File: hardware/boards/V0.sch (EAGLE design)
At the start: 100 parts, among them IC2 TPS6300, J1 SJ-43515TS-SMT, J2 HIROSE_DM3BT-DSF-PEJSHIROSE_D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, J3 MOLEX_105450-0101MOLEX_105450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, Q1 MC-306, Q2 ON_SEMI_MMBT5551LT1GON_SEMI_M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, U1 VS1053-L, U2 MICROCHIP_MCP73831T-2ATI-OTMI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, X1 PG203J, X3 FH12-45S-0.5SH

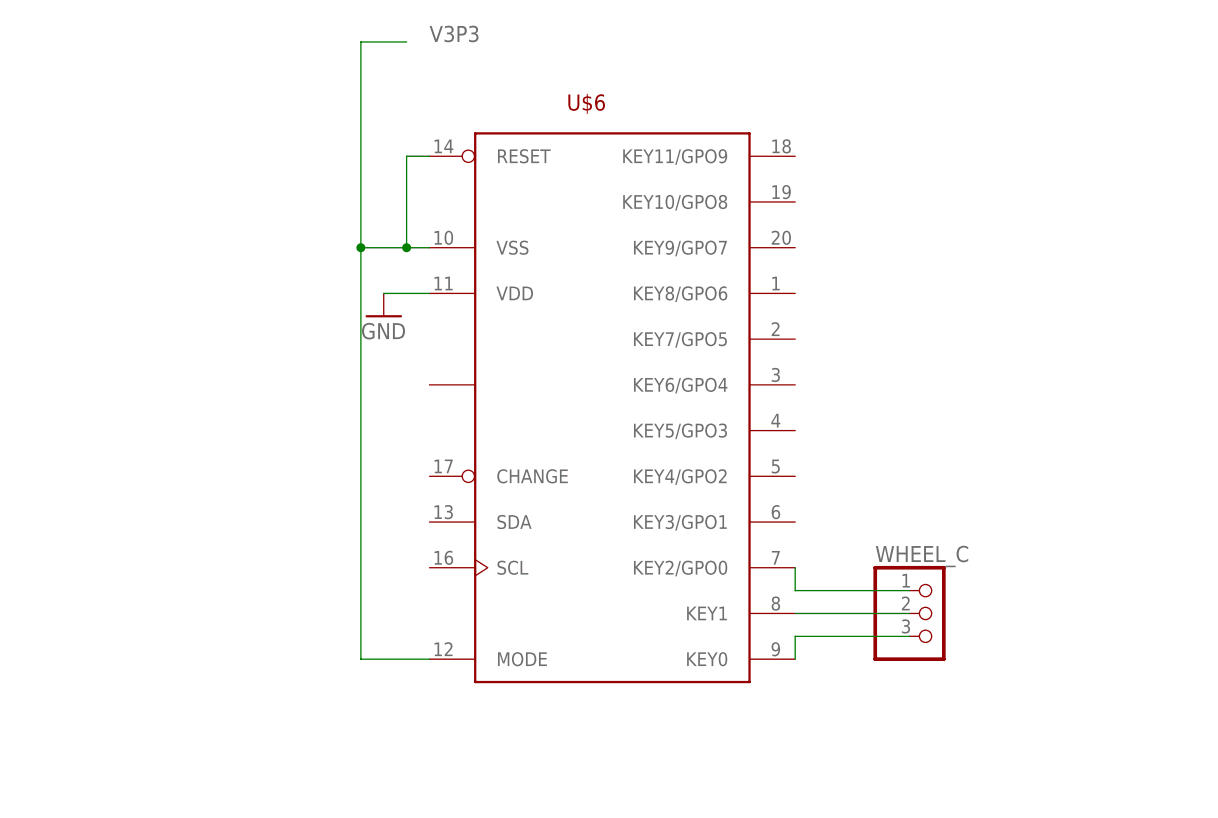
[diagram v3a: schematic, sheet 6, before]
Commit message: misc VS1053 fixes + fix/wire ATQ
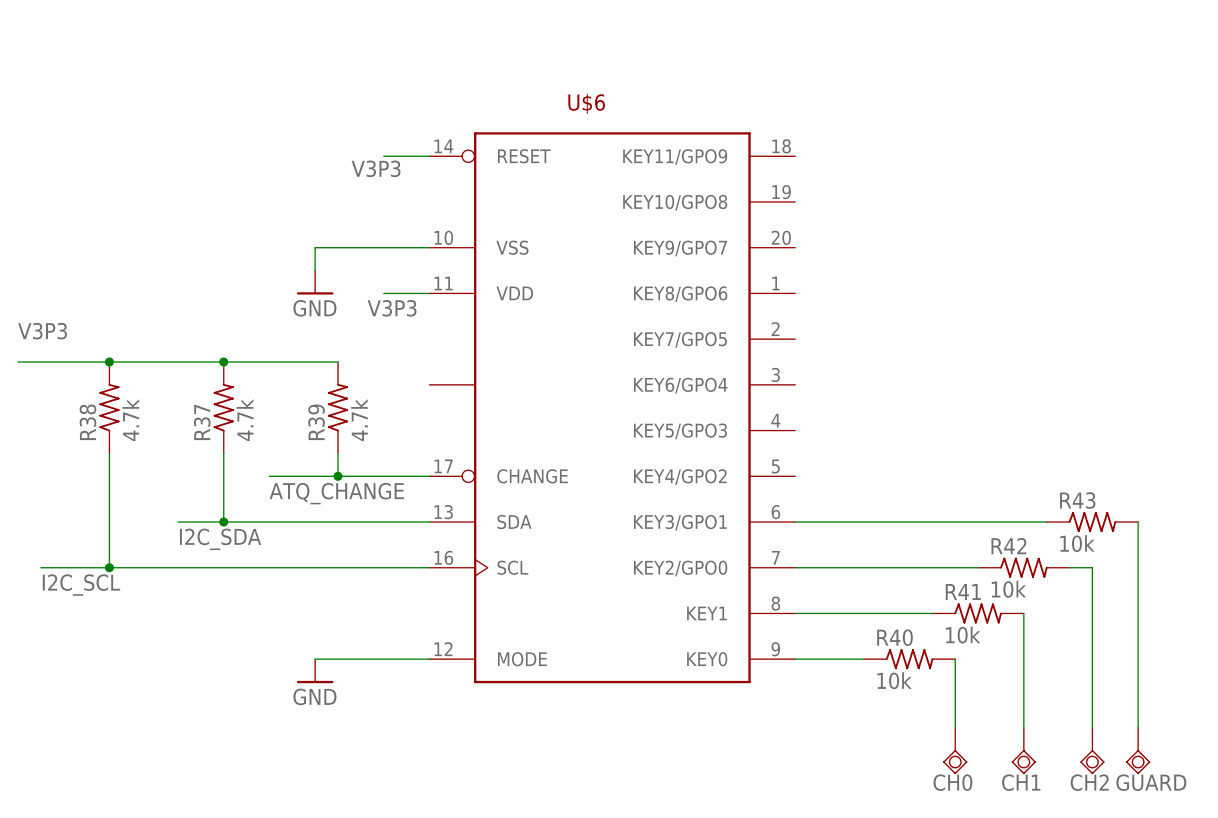
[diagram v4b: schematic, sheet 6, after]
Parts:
- removed WHEEL_C: (no value), pinhead:PINHD-1X3/90
- added C28, C29: 10uF, rcl:CPOL-USC/6032-28R
- added CH0, CH1, CH2, GUARD: TPSQTP20SQ, testpad:TPSQTP20SQ
- added R37, R38, R39: 4.7k, rcl:R-US_R0805
- added R40, R41, R42, R43: 10k, rcl:R-US_R0805
- C15, C16, C17, C18, C19, C20: value (none) -> 100nF
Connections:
- removed net +3V3: C15.1, C16.1, C17.1, U1P.AVDD, U1P.AVDD@1, U1P.AVDD@2, U1P.CVDD, U1P.CVDD@1, U1P.CVDD@2, U1P.CVDD@3
- removed net N$27 (its old number): U$6.KEY2/GPO0, WHEEL_C.1
- removed net N$48: U1G$1.TX
- removed net VCCIO: C18.1, C19.1, C20.1, R17.2, U1G$1.TEST, U1P.IOVDD, U1P.IOVDD@1, U1P.IOVDD@2
- new net ATQ_CHANGE: R39.1, U$6.CHANGE
- new net I2C_SCL: R38.1, U$6.SCL
- new net I2C_SDA: R37.1, U$6.SDA
- new net N$11: R40.1, U$6.KEY0
- new net N$18: CH1.TP, R41.2
- new net N$20: CH2.TP, R42.2
- new net N$23: R41.1, U$6.KEY1
- new net N$37: CH0.TP, R40.2
- new net N$40: GUARD.TP, R43.2
- net GND: now also C28.-, C29.-, U$6.MODE, U$6.VSS; no longer U$6.VDD
- net N$25: now also R42.1, U$6.KEY2/GPO0; no longer U$6.KEY0, WHEEL_C.3
- net N$26: now also R43.1, U$6.KEY3/GPO1; no longer U$6.KEY1, WHEEL_C.2
- net V1P8: now also C18.1, C19.1, C20.1, C28.+, U1P.CVDD, U1P.CVDD@1, U1P.CVDD@2, U1P.CVDD@3
- net V3P3: now also C15.1, C16.1, C17.1, C29.+, R17.2, R37.2, R38.2, R39.2, U$6.VDD, U1G$1.TEST, U1P.AVDD, U1P.AVDD@1, U1P.AVDD@2, U1P.IOVDD, U1P.IOVDD@1, U1P.IOVDD@2; no longer U$6.MODE, U$6.VSS
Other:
- moved on the sheet: C9, Q1

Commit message: inline + tip switch (bad) + ??
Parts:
- removed X1: PG203J, con-hirschmann:PG203J
- added R44: 10K, rcl:R-US_R0805
- added R45: 50k, rcl:R-US_R0805
- C12: value 10nF -> 47nF
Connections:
- removed net N$30: R13.1, U1G$1.GBUF, X1.2
- removed net N$31: R14.1, U1G$1.RIGHT, X1.1
- new net N$48: J1.RING2, R13.1, U1G$1.GBUF
- new net N$49: J1.RING1, R14.1, U1G$1.RIGHT
- new net TRRS_INLINE_CTRL: J1.SLEEVE, R44.1, U$1.IO35
- new net TRRS_TIP_SW: J1.TIP_SWITCH, R45.1, U$1.SENSOR_VP
- net GND: now also R45.2; no longer X1.3, X1.4
- net N$33: now also J1.TIP; no longer X1.5
- net V3P3: now also R44.2

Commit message: antenna and its very specific friends
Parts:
- removed Q1: MC-306, crystal:MC-306
- added C30: 2.7pF, rcl:C-USC0201
- added C31: 4.7pF, rcl:C-USC0201
- added U$4: ECS12P88MHZ, Crystal:ECS12P88MHZ
- added U$7: 1.6nH, L-0402:L-0402
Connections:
- new net N$30: ANT1.RF_FEED, C30.1, U$7.1
- new net N$31: C31.1, U$1.LNA_IN, U$7.2
- net GND: now also C30.2, C31.2, U$4.GND, U$4.GND2
- net N$21: now also U$4.IN/OUT; no longer Q1.1
- net N$4: now also U$4.IN/OUT2; no longer Q1.2

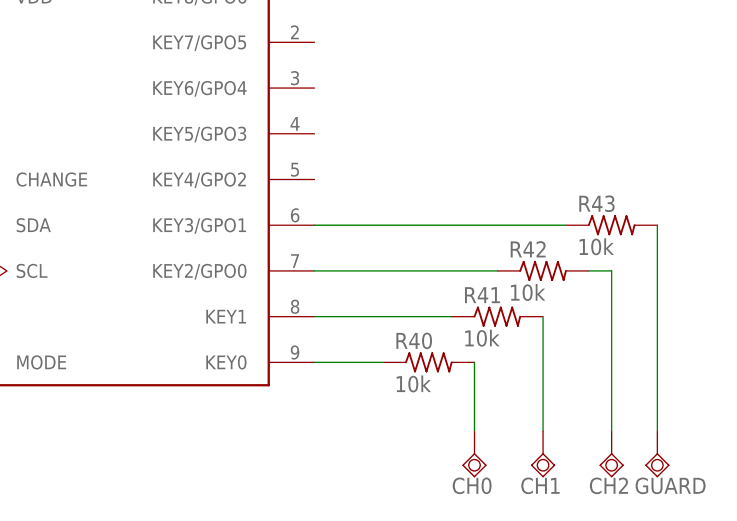
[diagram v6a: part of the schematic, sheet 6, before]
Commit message: added testpads
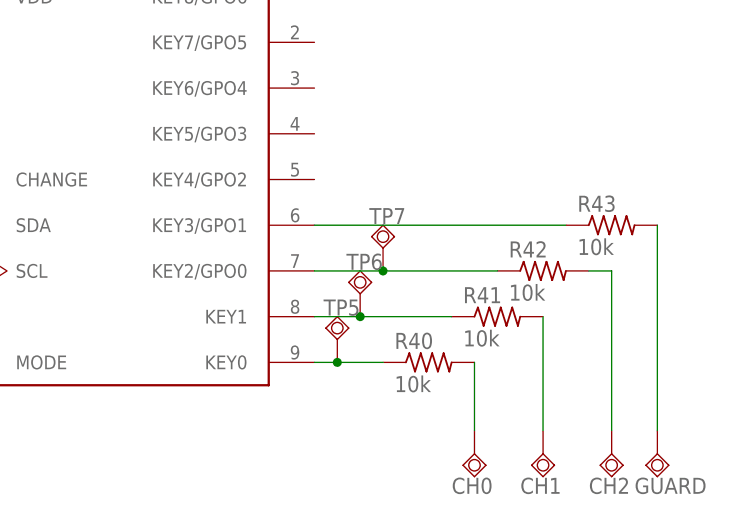
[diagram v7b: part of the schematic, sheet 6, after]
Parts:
- added TP1, TP2, TP3, TP4, TP5, TP6, TP7, TP8: TPSQTP15SQ, testpad:TPSQTP15SQ
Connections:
- removed net N$33: J1.TIP, R15.1, U1G$1.LEFT
- new net N$57: J1.TIP, R15.1, TP3.TP, U1G$1.LEFT
- net N$1: now also TP8.TP
- net N$11: now also TP5.TP
- net N$23: now also TP6.TP
- net N$25: now also TP7.TP
- net N$48: now also TP4.TP
- net V1P8: now also TP2.TP
- net V3P3: now also TP1.TP

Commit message: just the pinmap left!!
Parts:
- added C32, C33: (no value), rcl:C-USC1206
- added C34: 0.1uF, rcl:C-USC1206
- added Q1, Q3: (no value), semicon-smd-ipc:NPN-TRANSISTOR_SOT23
- added R46, R47: 1k, rcl:R-US_R0805
- added R48, R49: 10k, rcl:R-US_R0805
- added R50: 10K, rcl:R-US_R0805
- R12: device rcl:R-US_1812X7R -> rcl:R-US_R0805
- R13, R14, R15, R3: device rcl:R-US_01005 -> rcl:R-US_R0805
- R36: value (none) -> 50
- R8: device adafruit:R-US_R0603 -> rcl:R-US_R0805
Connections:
- new net DSR: JL.DSR
- new net DTR: JL.DTR, Q3.E, R48.1
- new net EN: C34.1, Q1.C, R50.1, U$1.EN
- new net IO0: Q3.C, U$1.IO0
- new net N$58: Q1.B, R48.2
- new net N$59: Q3.B, R49.2
- new net RTS: JL.RTS, Q1.E, R49.1
- new net RXD: JL.RXD, R46.2
- new net RXD0: R47.2, U$1.U0RXD
- new net TXD: JL.TXD, R47.1
- new net TXD0: R46.1, U$1.U0TXD
- net GND: now also C32.2, C33.2, C34.2, JL.GND_0, JL.GND_1, U$1.GND
- net V3P3: now also C32.1, C33.1, R50.2, U$1.VDD3P3_CPU, U$1.VDD3P3_RTC, U$1.VDDA3P3_1, U$1.VDDA3P3_2, U$1.VDDA_1, U$1.VDDA_2, U$1.VDDA_3
